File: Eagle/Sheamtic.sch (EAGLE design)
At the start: 16 parts, among them IC1 PIC16F874P

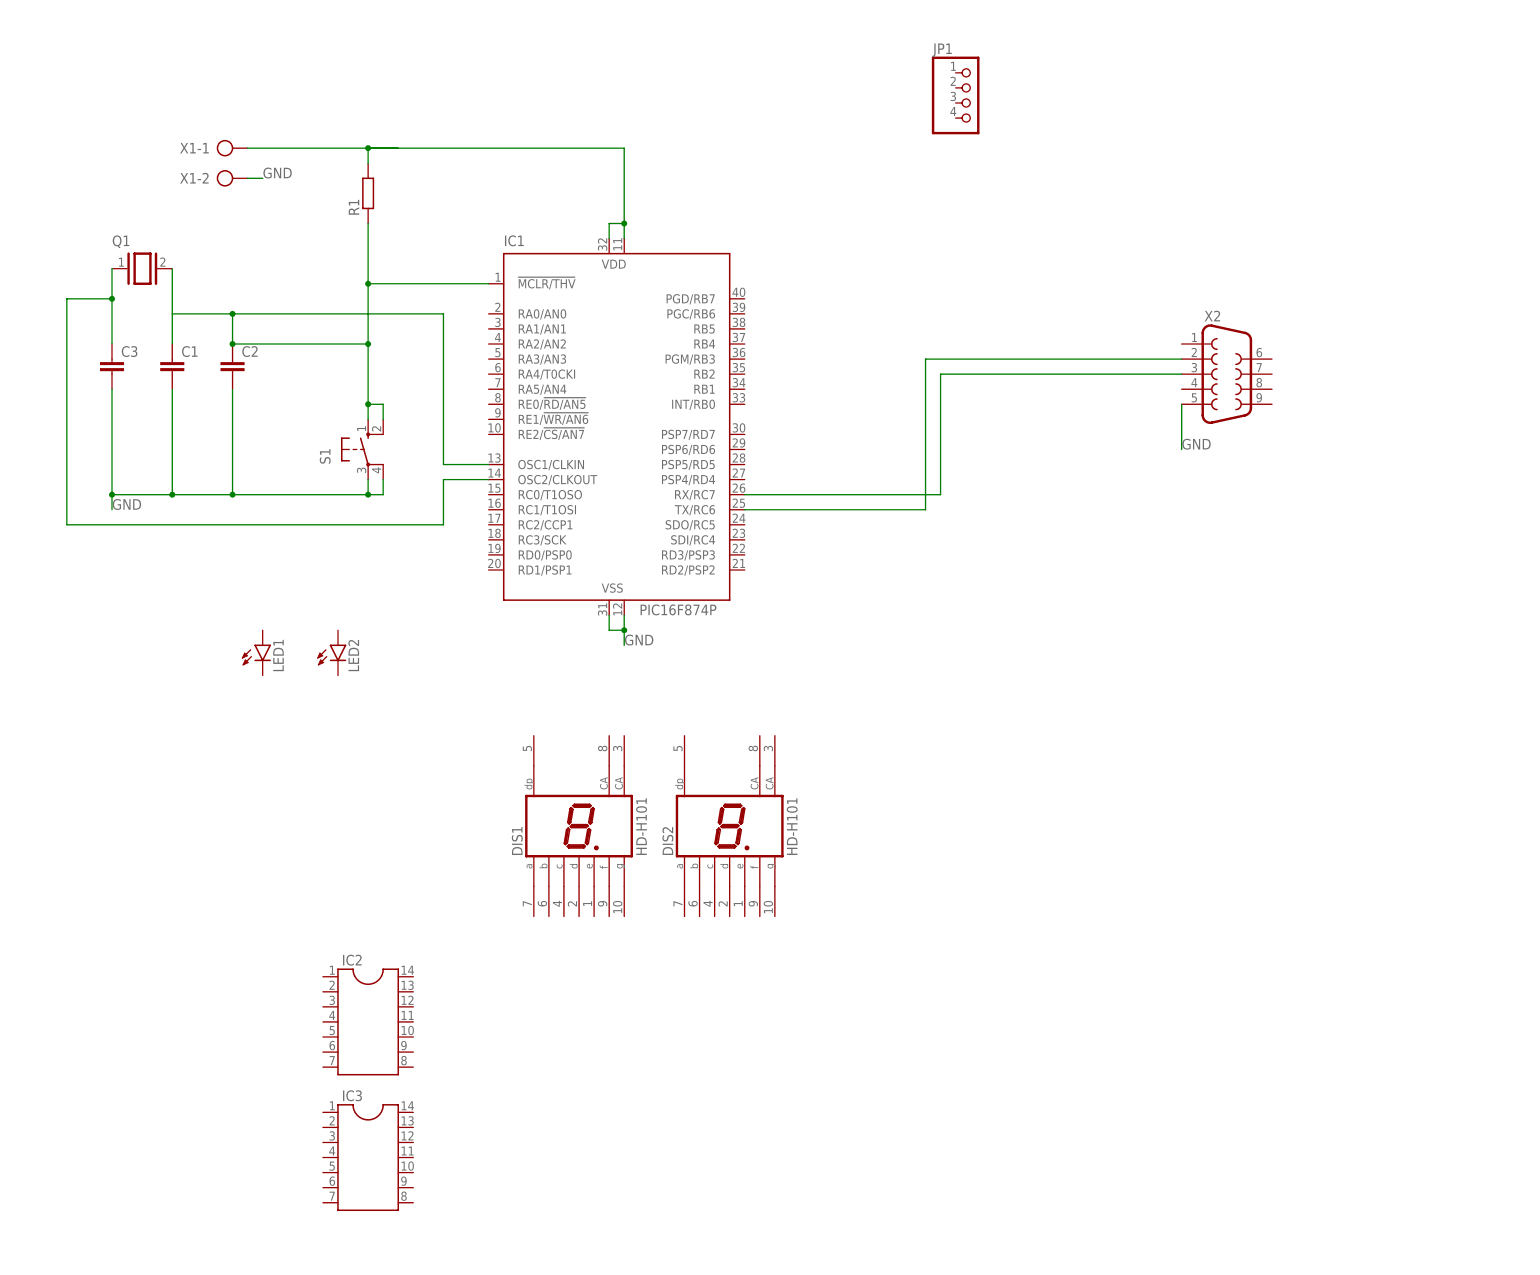
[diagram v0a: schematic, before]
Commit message: Add files via upload
Cablage, voir afficheur 7 seg car pas logique nombre entrée/sortie diff par rapport à proteus
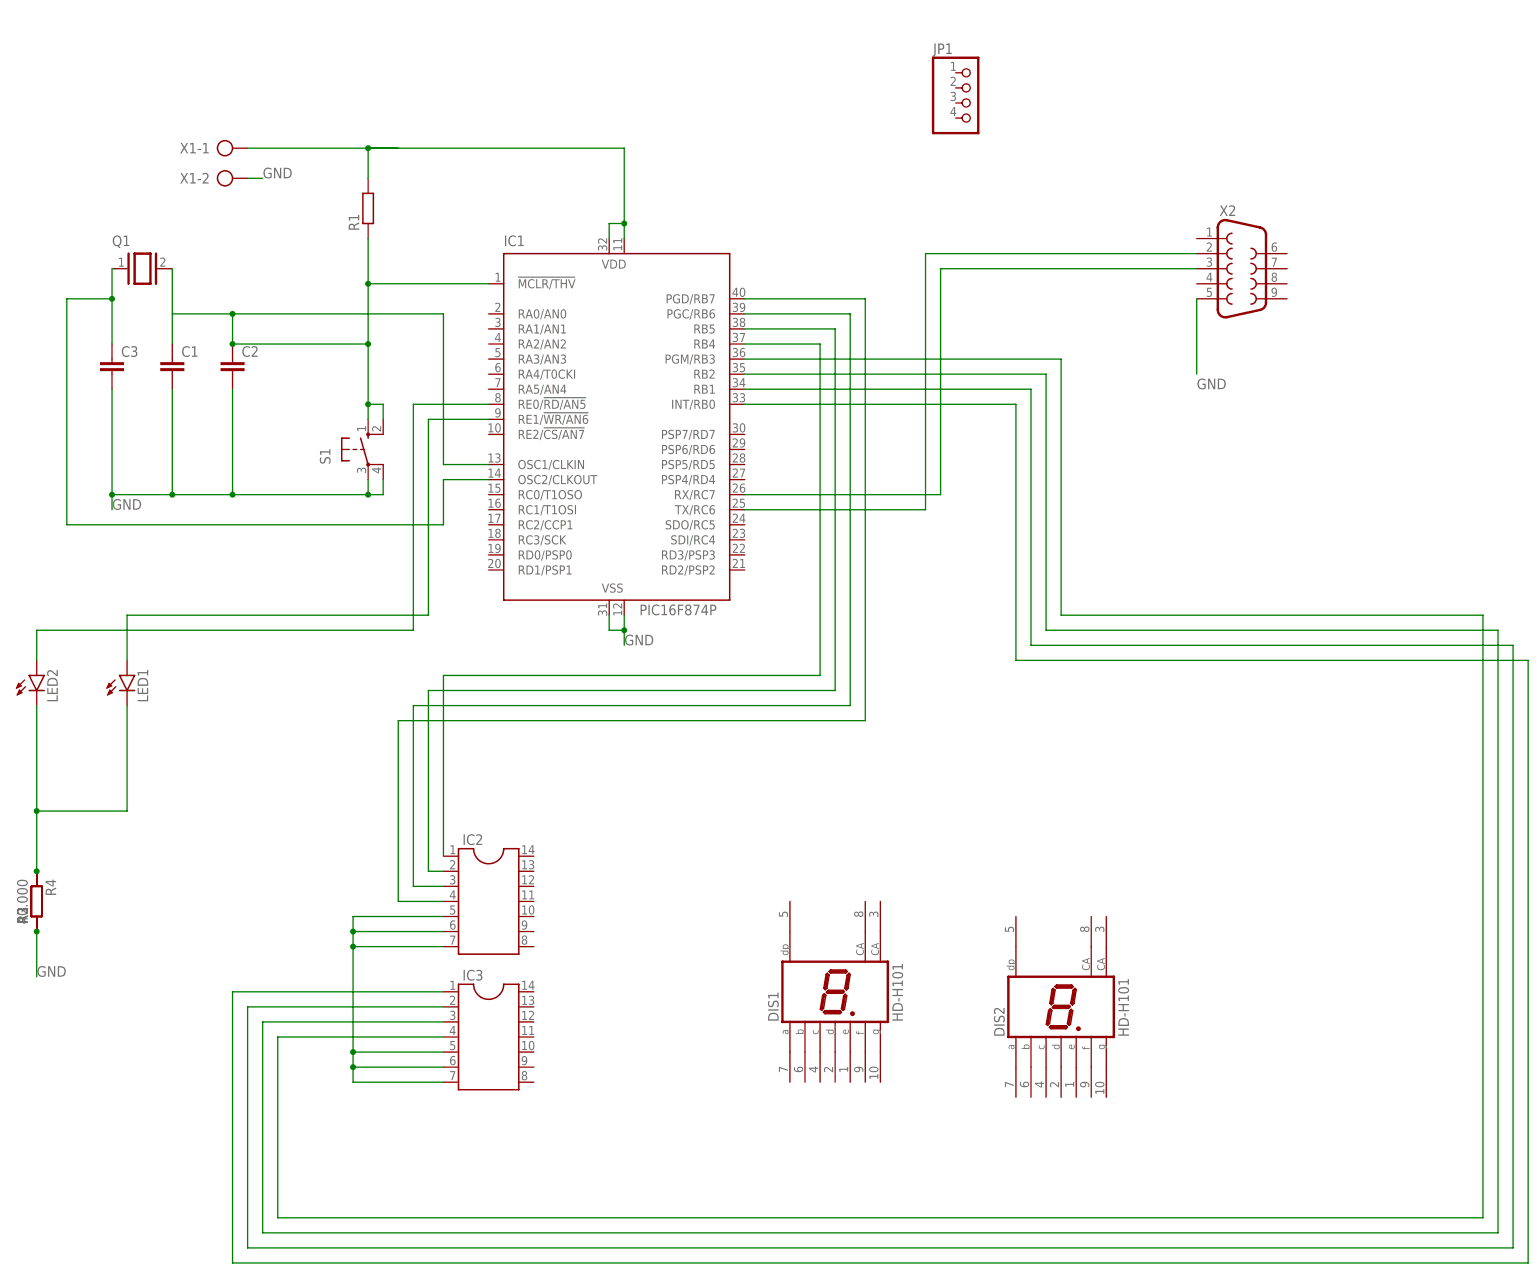
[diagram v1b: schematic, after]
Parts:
- added R2, R3: (no value), rcl:R-EU_0204/7
- added R4: 40.000, rcl:R-EU_0204/7
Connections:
- new net N$10: IC1.PGC/RB6, IC2.3
- new net N$11: IC1.INT/RB0, IC3.1
- new net N$12: IC1.PGD/RB7, IC2.4
- new net N$13: IC1.RB1, IC3.2
- new net N$14: IC1.RB2, IC3.3
- new net N$15: IC1.PGM/RB3, IC3.4
- new net N$16: IC1.RE0/!RD/AN5, LED2.A
- new net N$17: IC1.RE1/!WR/AN6, LED1.A
- new net N$18: LED1.C, LED2.C, R2.2, R3.2, R4.1
- new net N$3: IC2.5, IC2.6, IC2.7, IC3.5, IC3.6, IC3.7
- new net N$4: IC1.RB4, IC2.1
- new net N$8: IC1.RB5, IC2.2
- net GND: now also R2.1, R3.1, R4.2
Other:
- moved on the sheet: DIS1, DIS2, IC2, IC3, LED1, LED2, R1, X2

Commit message: Eagle
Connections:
- new net N$19: DIS1.B, IC2.13
- new net N$20: DIS1.C, IC2.12
- new net N$21: DIS1.D, IC2.11
- new net N$22: DIS1.E, IC2.10
- new net N$23: DIS1.F, IC2.9
- new net N$24: DIS1.G, IC2.8
- new net N$25: DIS2.A, IC3.14
- new net N$26: DIS2.B, IC3.13
- new net N$27: DIS2.C, IC3.12
- new net N$28: DIS2.D, IC3.11
- new net N$29: DIS2.E, IC3.10
- new net N$30: DIS2.F, IC3.9
- new net N$31: DIS2.G, IC3.8
- new net N$32: IC1.RC1/T1OSI, JP1.3
- new net VCC: DIS1.DP, DIS2.DP, IC1.VDD, IC1.VDD@1, IC2.5, IC2.6, IC2.7, IC3.5, IC3.6, IC3.7, JP1.4, R1.2, X1-1.KL
- net GND: now also DIS1.CA, DIS1.CA@1, DIS2.CA, DIS2.CA@1, JP1.1
- net N$1: now also DIS1.A, IC2.14; no longer IC1.VDD, IC1.VDD@1, R1.2, X1-1.KL
- net N$3: now also IC1.RC0/T1OSO, JP1.2; no longer IC2.5, IC2.6, IC2.7, IC3.5, IC3.6, IC3.7
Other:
- moved on the sheet: DIS1, DIS2, IC3

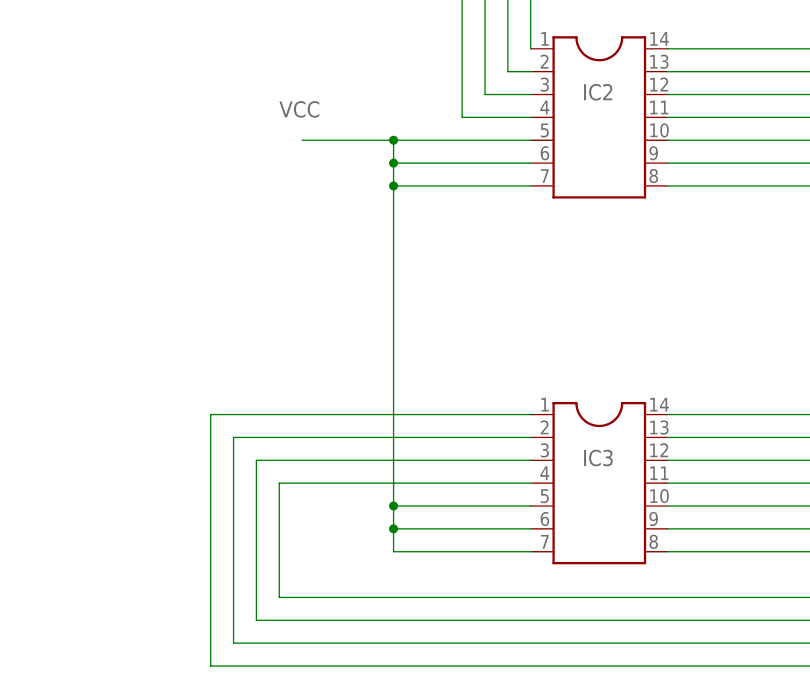
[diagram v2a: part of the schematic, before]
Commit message: correction proteus/eagle + test pic ccs
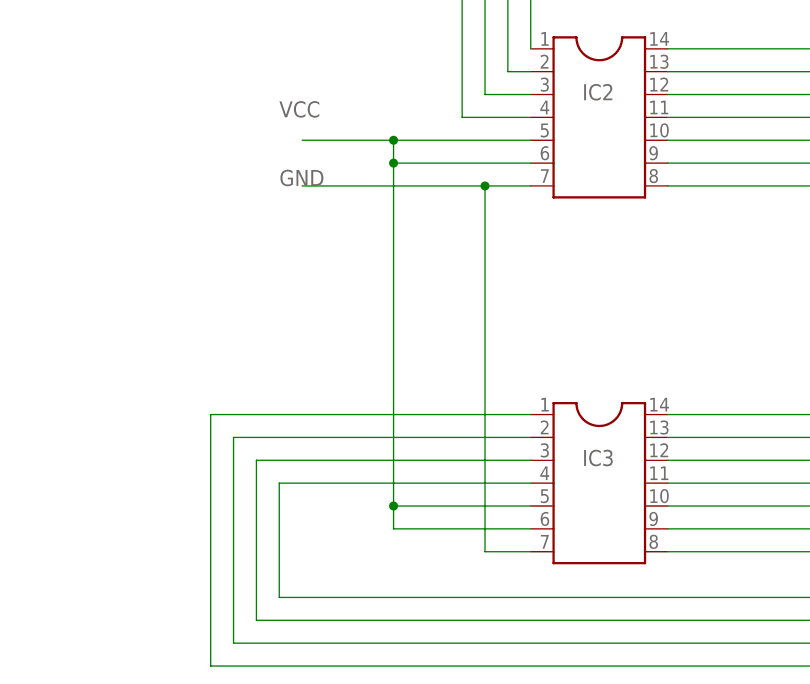
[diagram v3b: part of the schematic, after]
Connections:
- net GND: now also IC2.7, IC3.7
- net VCC: no longer IC2.7, IC3.7
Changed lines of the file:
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@@
 </segment>
 <segment>
-<pinref part="IC3" gate="G$1" pin="7"/>
-<wire x1="43.18" y1="-93.98" x2="27.94" y2="-93.98" width="0.1524" layer="91"/>
-<wire x1="27.94" y1="-93.98" x2="27.94" y2="-91.44" width="0.1524" layer="91"/>
-<pinref part="IC2" gate="G$1" pin="7"/>
 <wire x1="27.94" y1="-91.44" x2="27.94" y2="-88.9" width="0.1524" layer="91"/>
-<wire x1="27.94" y1="-88.9" x2="27.94" y2="-53.34" width="0.1524" layer="91"/>
-<wire x1="27.94" y1="-53.34" x2="43.18" y2="-53.34" width="0.1524" layer="91"/>
-<junction x="27.94" y="-53.34"/>
+<wire x1="27.94" y1="-88.9" x2="27.94" y2="-50.8" width="0.1524" layer="91"/>
 <pinref part="IC2" gate="G$1" pin="5"/>
-<wire x1="27.94" y1="-53.34" x2="27.94" y2="-50.8" width="0.1524" layer="91"/>
 <wire x1="27.94" y1="-50.8" x2="27.94" y2="-48.26" width="0.1524" layer="91"/>
 <wire x1="27.94" y1="-48.26" x2="43.18" y2="-48.26" width="0.1524" layer="91"/>
@@
 <pinref part="IC3" gate="G$1" pin="6"/>
 <wire x1="27.94" y1="-91.44" x2="43.18" y2="-91.44" width="0.1524" layer="91"/>
-<junction x="27.94" y="-91.44"/>
 <pinref part="IC3" gate="G$1" pin="5"/>
 <wire x1="43.18" y1="-88.9" x2="27.94" y2="-88.9" width="0.1524" layer="91"/>
@@
 <label x="121.92" y="101.6" size="1.778" layer="95"/>
 </segment>
+<segment>
+<pinref part="IC3" gate="G$1" pin="7"/>
+<wire x1="43.18" y1="-93.98" x2="38.1" y2="-93.98" width="0.1524" layer="91"/>
+<pinref part="IC2" gate="G$1" pin="7"/>
+<wire x1="43.18" y1="-53.34" x2="38.1" y2="-53.34" width="0.1524" layer="91"/>
+<wire x1="38.1" y1="-53.34" x2="17.78" y2="-53.34" width="0.1524" layer="91"/>
+<wire x1="38.1" y1="-93.98" x2="38.1" y2="-53.34" width="0.1524" layer="91"/>
+<junction x="38.1" y="-53.34"/>
+<label x="15.24" y="-53.34" size="1.778" layer="95"/>
+</segment>
 </net>

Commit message: eagle update
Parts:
- added R5, R6: (no value), rcl:R-EU_0204/7
- R4: value 40.000 -> (none)
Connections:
- new net N$34: DIS1.DP, IC1.RE2/!CS/AN7
- new net N$35: DIS2.CA, DIS2.CA@1, R6.1
- net GND: now also C1.1, C2.1, C3.1, R5.1, R5.2, R6.2; no longer C1.2, C2.2, C3.2, DIS2.CA, DIS2.CA@1
- net N$2: now also C2.2; no longer C2.1, IC1.OSC1/CLKIN
- net N$5: now also C3.2; no longer C3.1
- net N$9: now also C1.2, IC1.OSC1/CLKIN; no longer C1.1
- net VCC: no longer DIS1.DP, DIS2.DP
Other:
- moved on the sheet: C1, C2, C3
